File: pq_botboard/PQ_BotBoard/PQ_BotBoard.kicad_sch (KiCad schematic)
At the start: 37 parts, among them IC1 TCN75AVOA713, J1 53261-1471, J2 Conn_01x08_MountingPin, J3 53261-0271, U1 TPS7A7002DDAR

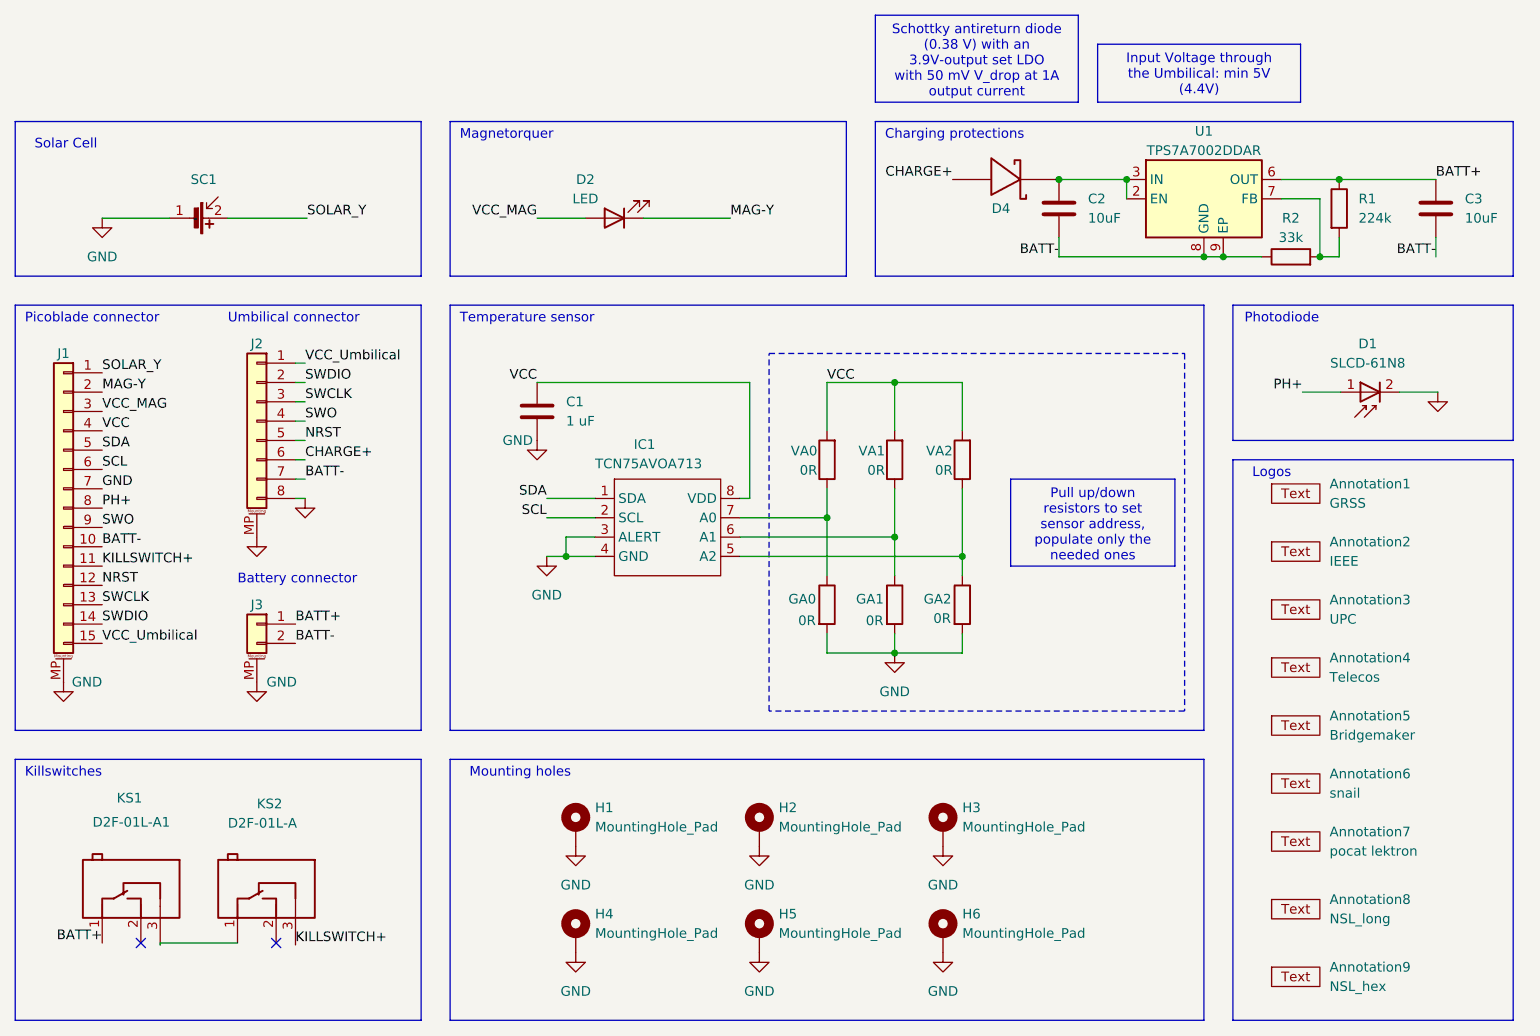
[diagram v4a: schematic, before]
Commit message: Recenter components to fit inside the square hole of the slider, change PicoBlade from 2 pins to 3 pins
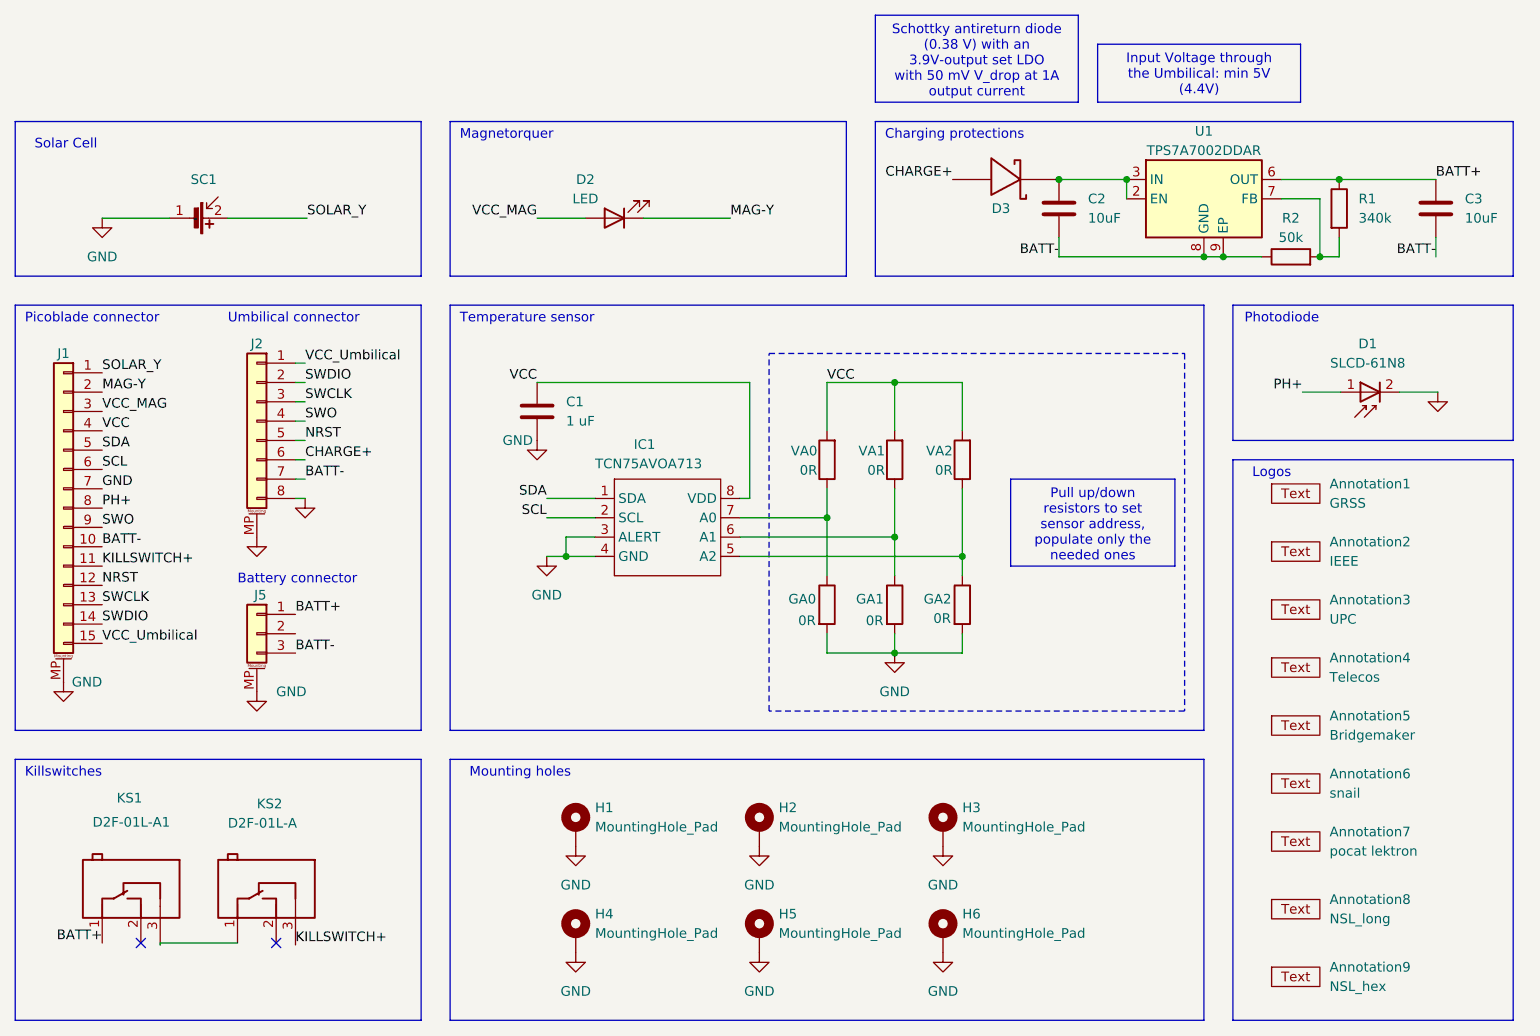
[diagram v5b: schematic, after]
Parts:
- removed J3: 53261-0271, Connector_Molex:Molex_PicoBlade_53261-0271_1x02-1MP_P1.25mm_Horizontal, symbol Connector_Generic_MountingPin:Conn_01x02_MountingPin
- added J5: Conn_01x03_MountingPin, Connector_Molex:Molex_PicoBlade_53261-0371_1x03-1MP_P1.25mm_Horizontal, symbol Connector_Generic_MountingPin:Conn_01x03_MountingPin
- R1: value 224k -> 340k
- R2: value 33k -> 50k
- renumbered D4 to D3
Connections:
- net BATT+: now also J5.1 (Pin_1)
- net BATT-: now also J5.3 (Pin_3)
- net GND: now also J5.MP (MountPin)
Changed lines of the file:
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@@
     (effects (font (size 1.27 1.27)) (justify left bottom))
   )
-  (label "BATT+" (at 113.03 104.14 0) (fields_autoplaced)
+  (label "BATT+" (at 113.03 102.87 0) (fields_autoplaced)
     (effects (font (size 1.27 1.27)) (justify left bottom))
   )
@@
     (effects (font (size 1.27 1.27)) (justify left bottom))
   )
-  (label "BATT-" (at 113.03 106.68 0) (fields_autoplaced)
+  (label "BATT-" (at 113.03 107.95 0) (fields_autoplaced)
     (effects (font (size 1.27 1.27)) (justify left bottom))
   )
@@
         (path "/e40a5bef-c31a-474e-b379-53d1d13d8a60"
           (reference "#PWR0109") (unit 1)
-        )
-      )
-    )
-  )
-  (symbol (lib_id "Connector_Generic_MountingPin:Conn_01x02_MountingPin") (at 107.95 104.14 0) (mirror y) (unit 1)
-    (in_bom yes) (on_board yes) (dnp no) (fields_autoplaced)
-    (property "Reference" "J3" (at 107.95 101.6 0)
-      (effects (font (size 1.27 1.27)))
-    )
-    (property "Value" "53261-0271" (at 106.6801 101.6 90)
-      (effects (font (size 1.27 1.27)) (justify left) hide)
-    )
-    (property "Footprint" "Connector_Molex:Molex_PicoBlade_53261-0271_1x02-1MP_P1.25mm_Horizontal" (at 107.95 104.14 0)
-      (effects (font (size 1.27 1.27)) hide)
-    )
-    (property "Datasheet" "~" (at 107.95 104.14 0)
-      (effects (font (size 1.27 1.27)) hide)
-    )
-    (property "BOM_SUPPLIER" "LCSC" (at 107.95 104.14 0)
-      (effects (font (size 1.27 1.27)) (justify left bottom) hide)
-    )
-    (property "BOM_SUPPLIER PART" "C189700" (at 107.95 104.14 0)
-      (effects (font (size 1.27 1.27)) (justify left bottom) hide)
-    )
-    (property "BOM_MANUFACTURER" "MOLEX" (at 107.95 104.14 0)
-      (effects (font (size 1.27 1.27)) (justify left bottom) hide)
-    )
-    (property "BOM_MANUFACTURER PART" "532610271" (at 107.95 104.14 0)
-      (effects (font (size 1.27 1.27)) (justify left bottom) hide)
-    )
-    (property "CONTRIBUTOR" "LCSC" (at 107.95 104.14 0)
-      (effects (font (size 1.27 1.27)) (justify left bottom) hide)
-    )
-    (property "BOM_JLCPCB PART CLASS" "Extended Part" (at 107.95 104.14 0)
-      (effects (font (size 1.27 1.27)) (justify left bottom) hide)
-    )
-    (property "SPICEPRE" "C" (at 107.95 104.14 0)
-      (effects (font (size 1.27 1.27)) (justify left bottom) hide)
-    )
-    (property "SPICESYMBOLNAME" "532610271" (at 107.95 104.14 0)
-      (effects (font (size 1.27 1.27)) (justify left bottom) hide)
-    )
-    (property "Manufacturer 1" "MOLEX" (at 107.95 104.14 0)
-      (effects (font (size 1.27 1.27)) hide)
-    )
-    (property "Manufacturer Part Number 1" "_PicoBlade_53261-0271" (at 107.95 104.14 0)
-      (effects (font (size 1.27 1.27)) hide)
-    )
-    (property "Supplier 1" "Mouser" (at 107.95 104.14 0)
-      (effects (font (size 1.27 1.27)) hide)
-    )
-    (property "Supplier Part Number 1" "538-53261-0271 " (at 107.95 104.14 0)
-      (effects (font (size 1.27 1.27)) hide)
-    )
-    (pin "1")
-    (pin "2")
-    (pin "MP")
-    (instances
-      (project "PQ_BotBoard"
-        (path "/e40a5bef-c31a-474e-b379-53d1d13d8a60"
-          (reference "J3") (unit 1)
         )
       )
@@
       (effects (font (size 1.27 1.27)) (justify left))
     )
-    (property "Value" "224k" (at 252.73 50.8 0)
+    (property "Value" "340k" (at 252.73 50.8 0)
       (effects (font (size 1.27 1.27)) (justify left))
     )
@@
     )
   )
+  (symbol (lib_id "Connector_Generic_MountingPin:Conn_01x03_MountingPin") (at 107.95 105.41 0) (mirror y) (unit 1)
+    (in_bom yes) (on_board yes) (dnp no)
+    (property "Reference" "J5" (at 109.22 100.33 0)
+      (effects (font (size 1.27 1.27)) (justify left))
+    )
+    (property "Value" "Conn_01x03_MountingPin" (at 105.41 107.0356 0)
+      (effects (font (size 1.27 1.27)) (justify left) hide)
+    )
+    (property "Footprint" "Connector_Molex:Molex_PicoBlade_53261-0371_1x03-1MP_P1.25mm_Horizontal" (at 107.95 105.41 0)
+      (effects (font (size 1.27 1.27)) hide)
+    )
+    (property "Datasheet" "~" (at 107.95 105.41 0)
+      (effects (font (size 1.27 1.27)) hide)
+    )
+    (pin "2")
+    (pin "1")
+    (pin "MP")
+    (pin "3")
+    (instances
+      (project "PQ_BotBoard"
+        (path "/e40a5bef-c31a-474e-b379-53d1d13d8a60"
+          (reference "J5") (unit 1)
+        )
+      )
+    )
+  )
   (symbol (lib_name "GND_7") (lib_id "power:GND") (at 114.3 87.63 0) (unit 1)
     (in_bom yes) (on_board yes) (dnp no)
@@
     )
   )
-  (symbol (lib_name "GND_8") (lib_id "power:GND") (at 107.95 111.76 0) (mirror y) (unit 1)
+  (symbol (lib_name "GND_8") (lib_id "power:GND") (at 107.95 113.03 0) (mirror y) (unit 1)
     (in_bom yes) (on_board yes) (dnp no)
-    (property "Reference" "#PWR0111" (at 107.95 118.11 0)
-      (effects (font (size 1.27 1.27)) hide)
-    )
-    (property "Value" "GND" (at 109.22 111.76 0)
+    (property "Reference" "#PWR0111" (at 107.95 119.38 0)
+      (effects (font (size 1.27 1.27)) hide)
+    )
+    (property "Value" "GND" (at 110.49 113.03 0)
       (effects (font (size 1.27 1.27)) (justify right))
     )
-    (property "Footprint" "" (at 107.95 111.76 0)
-      (effects (font (size 1.27 1.27)) hide)
-    )
-    (property "Datasheet" "" (at 107.95 111.76 0)
+    (property "Footprint" "" (at 107.95 113.03 0)
+      (effects (font (size 1.27 1.27)) hide)
+    )
+    (property "Datasheet" "" (at 107.95 113.03 0)
       (effects (font (size 1.27 1.27)) hide)
     )
@@
   (symbol (lib_id "passive-nsl:RBS1LAM40ATR_Schottky") (at 205.74 45.72 0) (unit 1)
     (in_bom yes) (on_board yes) (dnp no)
-    (property "Reference" "D4" (at 205.74 49.53 0)
+    (property "Reference" "D3" (at 205.74 49.53 0)
       (effects (font (size 1.27 1.27)))
     )
@@
       (project "PQ_BotBoard"
         (path "/e40a5bef-c31a-474e-b379-53d1d13d8a60"
-          (reference "D4") (unit 1)
+          (reference "D3") (unit 1)
         )
       )
@@
       (effects (font (size 1.27 1.27)))
     )
-    (property "Value" "33k" (at 243.84 53.34 90)
-      (effects (font (size 1.27 1.27)))
-    )
+    (property "Value" "50k" (at 243.84 53.34 90)
+      (effects (font (size 1.27 1.27)))
+    )
